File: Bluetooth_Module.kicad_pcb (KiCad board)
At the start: 2 copper layers, 96.8 x 104.7 mm, 7 parts, among them U1 ESP32-C3-DevKitM-1

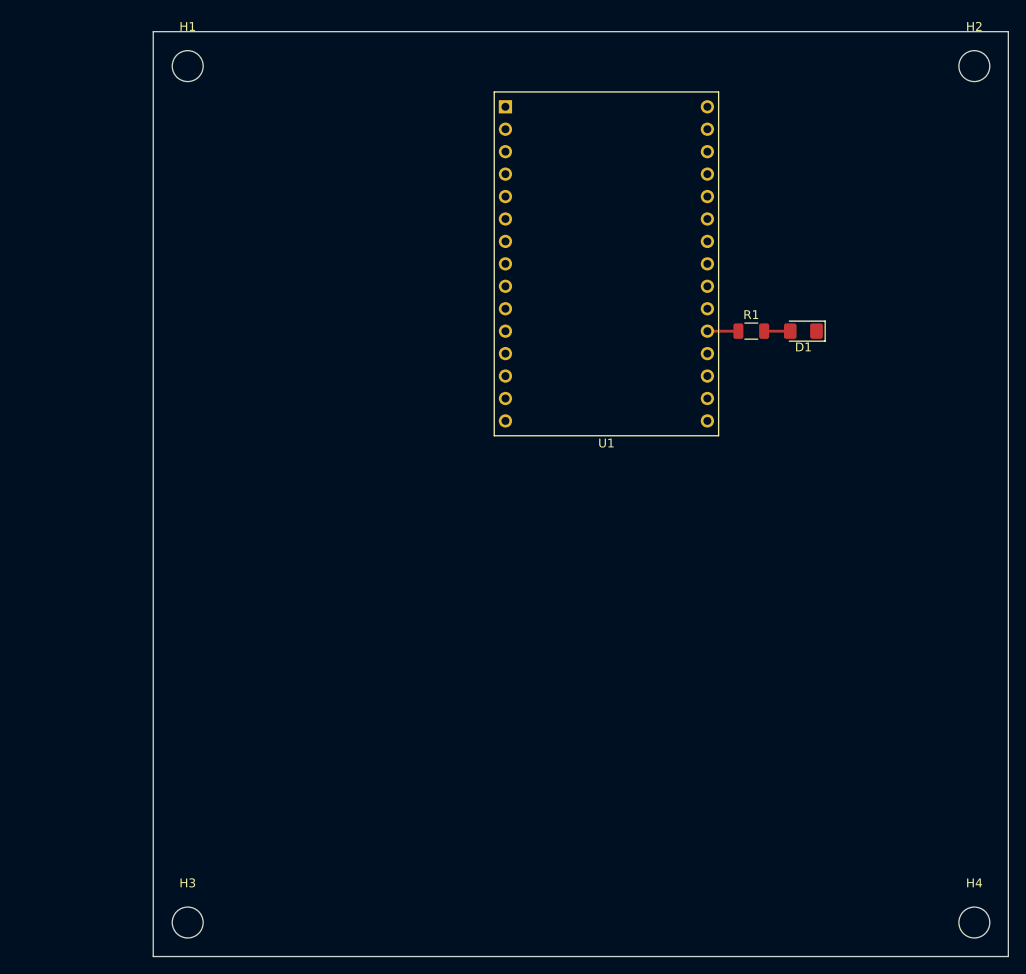
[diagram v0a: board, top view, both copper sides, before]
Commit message: Lesson 2 - transistor circuits added
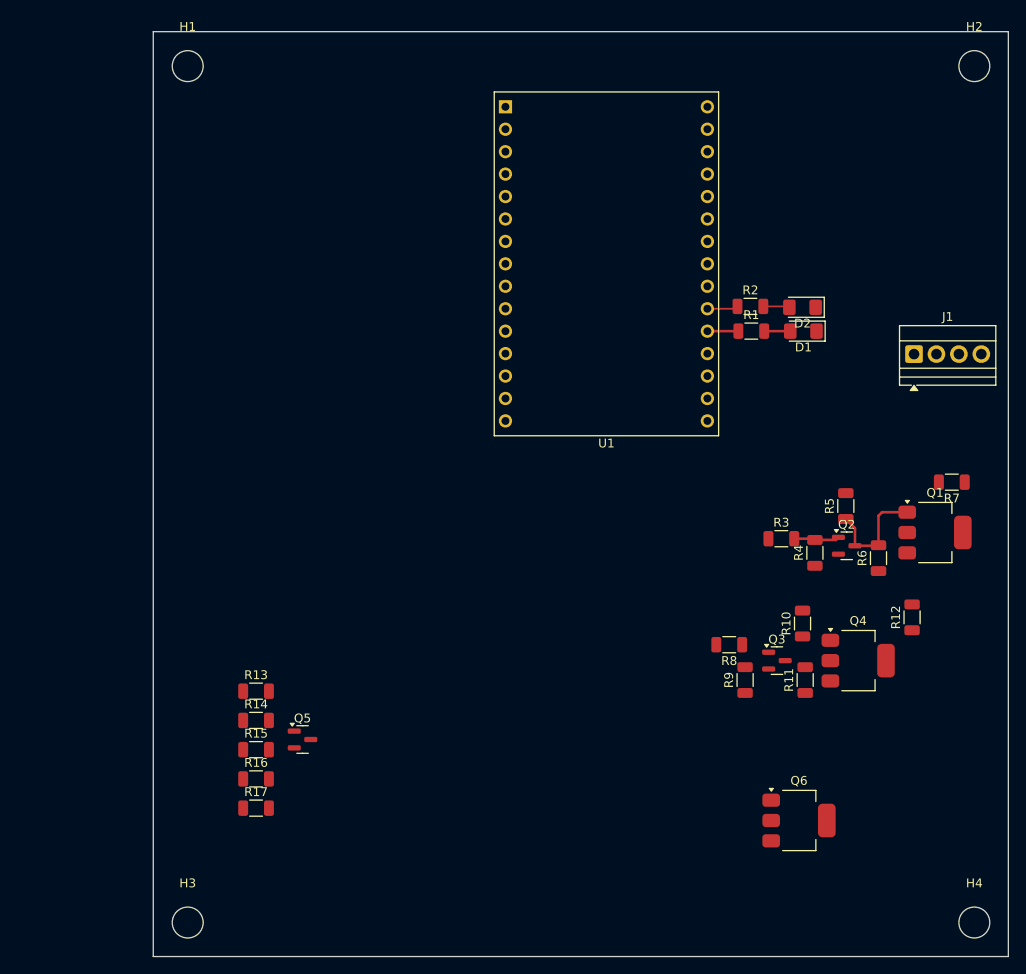
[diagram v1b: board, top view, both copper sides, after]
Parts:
- added D2: GREEN, LED_SMD:LED_1206_3216Metric_Pad1.42x1.75mm_HandSolder, F.Cu at (162.6, 84.3)
- added J1: Conn_01x04_Pin, TerminalBlock:TerminalBlock_Xinya_XY308-2.54-4P_1x04_P2.54mm_Horizontal, F.Cu at (175.2, 89.6)
- added Q1: STN3NF06, Package_TO_SOT_SMD:SOT-223-3_TabPin2, F.Cu at (177.6, 109.8)
- added Q2: BC817, Package_TO_SOT_SMD:SOT-23, F.Cu at (167.6, 111.3)
- added Q3: BC817, Package_TO_SOT_SMD:SOT-23, F.Cu at (159.7, 124.3)
- added Q4: STN3NF06, Package_TO_SOT_SMD:SOT-223-3_TabPin2, F.Cu at (168.9, 124.3)
- added Q5: BC817, Package_TO_SOT_SMD:SOT-23, F.Cu at (106.0, 133.2)
- added Q6: STN3NF06, Package_TO_SOT_SMD:SOT-223-3_TabPin2, F.Cu at (162.2, 142.4)
- added R10: 10k, Resistor_SMD:R_1206_3216Metric, F.Cu at (162.6, 120.1)
- added R11: 10k, Resistor_SMD:R_1206_3216Metric, F.Cu at (162.9, 126.5)
- added R12: 1k, Resistor_SMD:R_1206_3216Metric, F.Cu at (175.0, 119.4)
- added R13: 1k, Resistor_SMD:R_1206_3216Metric, F.Cu at (100.7, 127.8)
- added R14: 10k, Resistor_SMD:R_1206_3216Metric, F.Cu at (100.7, 131.1)
- added R15: 10k, Resistor_SMD:R_1206_3216Metric, F.Cu at (100.7, 134.4)
- added R16: 10k, Resistor_SMD:R_1206_3216Metric, F.Cu at (100.7, 137.7)
- added R17: 1k, Resistor_SMD:R_1206_3216Metric, F.Cu at (100.7, 141.0)
- added R2: 68R, Resistor_SMD:R_1206_3216Metric, F.Cu at (156.7, 84.2)
- added R3: 1k, Resistor_SMD:R_1206_3216Metric, F.Cu at (160.2, 110.5)
- added R4: 10k, Resistor_SMD:R_1206_3216Metric, F.Cu at (164.0, 112.1)
- added R5: 10k, Resistor_SMD:R_1206_3216Metric, F.Cu at (167.5, 106.8)
- added R6: 10k, Resistor_SMD:R_1206_3216Metric, F.Cu at (171.2, 112.7)
- added R7: 1k, Resistor_SMD:R_1206_3216Metric, F.Cu at (179.5, 104.1)
- added R8: 1k, Resistor_SMD:R_1206_3216Metric, F.Cu at (154.3, 122.5)
- added R9: 10k, Resistor_SMD:R_1206_3216Metric, F.Cu at (156.1, 126.5)
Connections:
- U1 pad 21: unconnected-(U1-IO5-Pad21) -> Net-(U1-IO5)
- U1 pad 22: unconnected-(U1-IO6-Pad22) -> LED_R
- U1 pad 23: unconnected-(U1-IO7-Pad23) -> LED_G
- U1 pad 25: unconnected-(U1-IO8-Pad25) -> LED_B
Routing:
- net Net-(Q1-G): track 0.00 -> 12.9 mm
- net Net-(Q2-B): track 0.00 -> 5.18 mm
- net Net-(U1-IO5): track 0.00 -> 3.52 mm
- net Net-(D2-A): track 0.00 -> 2.99 mm

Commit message: Lesson 4 - Power Supply
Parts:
- removed H2: MountingHole, MountingHole:MountingHole_3.5mm
- added C1: 100n/25V, Capacitor_SMD:C_1206_3216Metric, F.Cu at (103.4, 100.9)
- added C2: 100n/25V, Capacitor_SMD:C_1206_3216Metric, F.Cu at (112.3, 101.3)
- added C3: 22uF/35V, Capacitor_SMD:CP_Elec_5x5.8, F.Cu at (117.2, 100.5)
- added C4: 100n/25V, Capacitor_SMD:C_1206_3216Metric, F.Cu at (95.2, 92.7)
- added C5: 100n/25V, Capacitor_SMD:C_1206_3216Metric, F.Cu at (94.8, 63.3)
- added D3: D, Diode_SMD:D_SOD-123F, F.Cu at (143.1, 74.4)
- added D5: D_TVS_12V, Diode_SMD:D_SMA, F.Cu at (107.4, 100.5)
- added J2: Conn_01x01_Socket, MountingHole:MountingHole_3mm_Pad_Via, F.Cu at (129.9, 109.3)
- added J3: Conn_01x01_Socket, MountingHole:MountingHole_3mm_Pad_Via, F.Cu at (145.5, 109.5)
- added J4: Jack-DC, Connector_BarrelJack:BarrelJack_CUI_PJ-063AH_Horizontal, F.Cu at (95.3, 100.0)
- added K1: G2RL-1A-H, Relay_THT:Relay_SPST_Omron_G2RL-1A, F.Cu at (138.2, 78.6)
- added PS1: DPU01N-15, SPU01M:DPU01N15, F.Cu at (105.5, 106.9)
- added Q7: BC817, Package_TO_SOT_SMD:SOT-23, F.Cu at (133.4, 85.2)
- added R18: 1k, Resistor_SMD:R_1206_3216Metric, F.Cu at (120.3, 89.7)
- added R19: 10k, Resistor_SMD:R_1206_3216Metric, F.Cu at (120.3, 93.0)
- moved R17 94.9 mm to (139.6, 54.4), turned to 180 degrees
- moved Q6 85.3 mm to (139.5, 60.1), turned to 90 degrees
- moved R16 83.0 mm to (142.9, 66.2), turned to 180 degrees
- moved R15 78.1 mm to (143.0, 68.7), turned to 180 degrees
- moved Q5 73.5 mm to (137.4, 66.8), turned to 90 degrees
- moved R12 72.9 mm to (130.4, 61.7), turned to 180 degrees
- moved R7 71.9 mm to (121.4, 61.8)
- moved R14 71.3 mm to (137.7, 70.0), turned to 180 degrees
- moved Q1 70.2 mm to (121.4, 67.7), turned to 90 degrees
- moved Q4 68.7 mm to (130.0, 67.7), turned to 90 degrees
- moved R13 66.4 mm to (137.7, 72.7)
- moved H4 62.8 mm to (137.4, 109.8)
- moved R6 62.3 mm to (122.8, 73.5), turned to 180 degrees
- moved Q2 61.3 mm to (118.8, 74.3), turned to 90 degrees
- moved R11 61.1 mm to (132.1, 73.7), turned to 180 degrees
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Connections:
- net Net-(U1-5V-Pad13) renamed +5V
- R2 pad 1: Net-(U1-IO5) -> unconnected-(R2-Pad1)
- U1 pad 1: Net-(U1-GND-Pad1) -> GND
- U1 pad 12: Net-(U1-GND-Pad1) -> GND
- U1 pad 15: Net-(U1-GND-Pad1) -> GND
- U1 pad 16: Net-(U1-GND-Pad1) -> GND
- U1 pad 19: Net-(U1-GND-Pad1) -> GND
- U1 pad 2: Net-(U1-3V3-Pad2) -> +3V3
- U1 pad 21: Net-(U1-IO5) -> LED_R
- U1 pad 22: LED_R -> LED_G
- U1 pad 23: LED_G -> LED_B
- U1 pad 24: Net-(U1-GND-Pad1) -> GND
- U1 pad 25: LED_B -> unconnected-(U1-IO8-Pad25)
- U1 pad 27: Net-(U1-GND-Pad1) -> GND
- U1 pad 3: Net-(U1-3V3-Pad2) -> +3V3
- U1 pad 30: Net-(U1-GND-Pad1) -> GND
- U1 pad 6: Net-(U1-GND-Pad1) -> GND
- U1 pad 8: Net-(U1-GND-Pad1) -> GND
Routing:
- net +12V: track 0.00 -> 46.6 mm
- net Net-(J2-Pin_1): track 0.00 -> 14.2 mm
- net Net-(Q1-G): track 12.9 -> 0.00 mm
- net Net-(J3-Pin_1): track 0.00 -> 11.0 mm
- net Net-(Q2-B): track 5.18 -> 0.00 mm
- net Net-(U1-IO5): track 3.52 -> 0.00 mm
- net Net-(U1-IO4): track 3.51 -> 0.00 mm
- added copper zone on B.Cu, net GND
- added copper zone on F.Cu, net GND
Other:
- board size 96.8 x 104.7 mm -> 60.5 x 61.4 mm
- board text added: "For 230 VAC appliances (IEC 60335-1 typical case): Working voltage ≈ 250 V CTI ≥ 400 (FR-4 often MG II) Pollution Degree 2 Required reinforced creepage = 5.0 mm"
- board text added: "Obudowa Z54 KRADEX"
- board text removed: "Obudowa Z59J PSKRADEX"
